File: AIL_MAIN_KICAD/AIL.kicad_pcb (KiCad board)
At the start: 2 copper layers, 71.9 x 33.4 mm, 25 parts, among them IC1 LT8315, J1 Conn_01x02_Female, J2 Conn_01x02_Female

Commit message: Updating main board
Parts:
- removed J1: Conn_01x02_Female, 2155760-1002:215760-YY02
- added D10: LED, AIL_MAIN_FOOT:LEDC2012X100N, B.Cu at (141.7, 92.2)
- added D11: LED, AIL_MAIN_FOOT:LEDC2012X100N, B.Cu at (146.3, 92.2)
- added D12: LED, AIL_MAIN_FOOT:LEDC2012X100N, B.Cu at (150.9, 92.2)
- added D13: LED, AIL_MAIN_FOOT:LEDC2012X100N, B.Cu at (155.7, 92.2)
- added D14: LED, AIL_MAIN_FOOT:LEDC2012X100N, B.Cu at (160.3, 92.2)
- added D15: LED, AIL_MAIN_FOOT:LEDC2012X100N, B.Cu at (141.7, 89.2)
- added D16: LED, AIL_MAIN_FOOT:LEDC2012X100N, B.Cu at (146.3, 89.2)
- added D17: LED, AIL_MAIN_FOOT:LEDC2012X100N, B.Cu at (150.9, 89.2)
- added D18: LED, AIL_MAIN_FOOT:LEDC2012X100N, B.Cu at (155.7, 89.2)
- added D19: LED, AIL_MAIN_FOOT:LEDC2012X100N, B.Cu at (160.3, 89.2)
- added D20: LED, AIL_MAIN_FOOT:LEDC2012X100N, B.Cu at (141.7, 86.1)
- added D21: LED, AIL_MAIN_FOOT:LEDC2012X100N, B.Cu at (146.3, 86.1)
- added D22: LED, AIL_MAIN_FOOT:LEDC2012X100N, B.Cu at (150.9, 86.1)
- added D23: LED, AIL_MAIN_FOOT:LEDC2012X100N, B.Cu at (155.7, 86.1)
- added D24: LED, AIL_MAIN_FOOT:LEDC2012X100N, B.Cu at (160.3, 86.1)
- added D25: LED, AIL_MAIN_FOOT:LEDC2012X100N, B.Cu at (141.7, 83.1)
- added D26: LED, AIL_MAIN_FOOT:LEDC2012X100N, B.Cu at (146.3, 83.1)
- added D27: LED, AIL_MAIN_FOOT:LEDC2012X100N, B.Cu at (150.9, 83.1)
- added D28: LED, AIL_MAIN_FOOT:LEDC2012X100N, B.Cu at (155.7, 83.1)
- added D29: LED, AIL_MAIN_FOOT:LEDC2012X100N, B.Cu at (160.3, 83.1)
- added D5: LED, AIL_MAIN_FOOT:LEDC2012X100N, B.Cu at (141.7, 95.2)
- added D6: LED, AIL_MAIN_FOOT:LEDC2012X100N, B.Cu at (146.3, 95.2)
- added D7: LED, AIL_MAIN_FOOT:LEDC2012X100N, B.Cu at (150.9, 95.2)
- added D8: LED, AIL_MAIN_FOOT:LEDC2012X100N, B.Cu at (155.7, 95.2)
- added D9: LED, AIL_MAIN_FOOT:LEDC2012X100N, B.Cu at (160.3, 95.2)
- added R8: 20, Resistor_SMD:R_0603_1608Metric_Pad0.98x0.95mm_HandSolder, B.Cu at (131.6, 96.2)
- added REF1: MountingHole_3mm, MountingHole:MountingHole_3mm, F.Cu at (122.0, 92.0)
- added REF2: MountingHole_3mm, MountingHole:MountingHole_3mm, F.Cu at (178.0, 79.0)
- added REF3: MountingHole_3mm, MountingHole:MountingHole_3mm, F.Cu at (178.0, 105.0)
- J2: footprint 2155760-1002:215760-YY02 -> Connector_Molex:Molex_Micro-Fit_3.0_43045-0200_2x01_P3.00mm_Horizontal
- moved C9 73.0 mm to (165.9, 95.0)
- moved C7 68.3 mm to (180.1, 88.2)
- moved R7 68.3 mm to (177.2, 88.2)
- moved R6 68.2 mm to (174.5, 86.3)
- moved D4 67.8 mm to (165.6, 84.1)
- moved C6 66.3 mm to (174.6, 92.2)
- moved R4 66.3 mm to (173.1, 94.8)
- moved R5 66.3 mm to (171.4, 87.5)
- moved IC1 65.7 mm to (166.5, 90.3)
- moved C4 65.0 mm to (178.2, 94.1), turned to 90 degrees
- moved R1 64.9 mm to (155.2, 91.7)
- moved R3 64.2 mm to (169.4, 95.0)
- moved C5 63.0 mm to (161.8, 91.7), turned to -90 degrees
- moved C3 62.0 mm to (151.7, 92.6), turned to -90 degrees
- moved C8 62.0 mm to (156.2, 88.1), turned to -90 degrees
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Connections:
- net /12V renamed +12V
- IC1 pad 15: unconnected-(IC1-Pad15) -> ICGND
- IC1 pad 2: unconnected-(IC1-Pad2) -> HV1
- IC1 pad 3: unconnected-(IC1-Pad3) -> HV1
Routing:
- net GND: track 37.0 -> 82.3 mm
- net HV1: track 61.1 -> 39.0 mm, vias 2 -> 0
- net Net-(C3-Pad1): track 27.8 -> 11.6 mm, vias 2 -> 0
- net Net-(C9-Pad1): track 16.0 -> 5.27 mm, vias 2 -> 0
- net Net-(D10-Pad2): track 0.00 -> 9.09 mm
- net ICGND: track 85.1 -> 76.1 mm
- net HV3: track 16.6 -> 24.2 mm
- net +12V: track 33.2 -> 30.1 mm, vias 2 -> 1
- net Net-(C7-Pad1): track 14.4 -> 11.5 mm
- net Net-(D7-Pad1): track 0.00 -> 2.73 mm
- net Net-(D27-Pad1): track 0.00 -> 2.73 mm
- net Net-(D22-Pad1): track 0.00 -> 2.73 mm
- net Net-(D17-Pad1): track 0.00 -> 2.73 mm
- net Net-(D12-Pad1): track 0.00 -> 2.73 mm
- net Net-(D8-Pad1): track 0.00 -> 2.47 mm
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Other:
- board size 71.9 x 33.4 mm -> 68 x 38 mm

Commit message: updating with BOM
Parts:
- added C3: 22uF, Capacitor_SMD:C_0805_2012Metric_Pad1.18x1.45mm_HandSolder, F.Cu at (130.6, 97.0)
- C1: footprint Capacitor_SMD:C_0603_1608Metric_Pad1.08x0.95mm_HandSolder -> Capacitor_SMD:C_1812_4532Metric_Pad1.57x3.40mm_HandSolder
- C2: value 43E-6 -> 22uF; footprint Capacitor_SMD:C_0603_1608Metric_Pad1.08x0.95mm_HandSolder -> Capacitor_SMD:C_0805_2012Metric_Pad1.18x1.45mm_HandSolder
- C4: footprint Capacitor_SMD:C_0603_1608Metric_Pad1.08x0.95mm_HandSolder -> Capacitor_SMD:C_01005_0402Metric_Pad0.57x0.30mm_HandSolder
- C9: value 100E-9 -> 10E-6
- R6: value 1.91E6 -> 1.87E6; footprint Resistor_SMD:R_0603_1608Metric_Pad0.98x0.95mm_HandSolder -> Capacitor_SMD:C_1206_3216Metric_Pad1.33x1.80mm_HandSolder
- moved C7 18.8 mm to (167.7, 102.3), turned to 180 degrees
- moved C4 17.0 mm to (162.1, 99.3), turned to 0 degrees
- moved REF1 15.2 mm to (128.0, 106.0)
- moved R7 14.7 mm to (167.7, 99.5), turned to 0 degrees
- moved R4 12.0 mm to (161.1, 95.4), turned to 90 degrees
- moved C6 11.9 mm to (163.6, 96.9), turned to 0 degrees
- moved R6 11.1 mm to (170.2, 96.5), turned to 0 degrees
- moved R3 9.10 mm to (160.9, 91.7), turned to -90 degrees
- moved C9 8.45 mm to (160.9, 88.2), turned to -90 degrees
- moved C5 7.98 mm to (164.2, 84.1), turned to 180 degrees
- moved D4 7.30 mm to (171.8, 87.9), turned to 90 degrees
- moved R2 7.21 mm to (167.8, 84.1), turned to 180 degrees
- moved R5 6.33 mm to (169.4, 93.5), turned to 0 degrees
- moved IC1 1.76 mm to (165.6, 88.8), turned to 180 degrees
- moved C2 1.71 mm to (130.6, 94.5)
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- renumbered C3 to C10
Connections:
- C7 pad 1: Net-(C7-Pad1) -> Net-(D4-Pad1)
- IC1 pad 17: Net-(C7-Pad1) -> Net-(IC1-Pad17)
- R6 pad 1: Net-(C7-Pad1) -> Net-(IC1-Pad17)
- R7 pad 2: Net-(C7-Pad1) -> Net-(IC1-Pad17)
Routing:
- net HV3: track 24.2 -> 8.34 mm
- net ICGND: track 76.1 -> 61.7 mm
- net Net-(D10-Pad2): track 9.09 -> 21.3 mm
- net Net-(C7-Pad1): track 11.5 -> 0.00 mm
- net HV2: track 20.3 -> 11.6 mm
- net Net-(IC1-Pad17): track 0.00 -> 8.61 mm
- net Net-(D4-Pad1): track 7.45 -> 13.9 mm
- net HV1: track 39.0 -> 44.3 mm
- net GND: track 82.3 -> 80.2 mm
- net Net-(C4-Pad1): track 4.22 -> 3.20 mm
- net Net-(IC1-Pad18): track 2.09 -> 3.03 mm
- net Net-(C9-Pad1): track 5.27 -> 4.53 mm
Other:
- board size 68 x 38 mm -> 61 x 38 mm

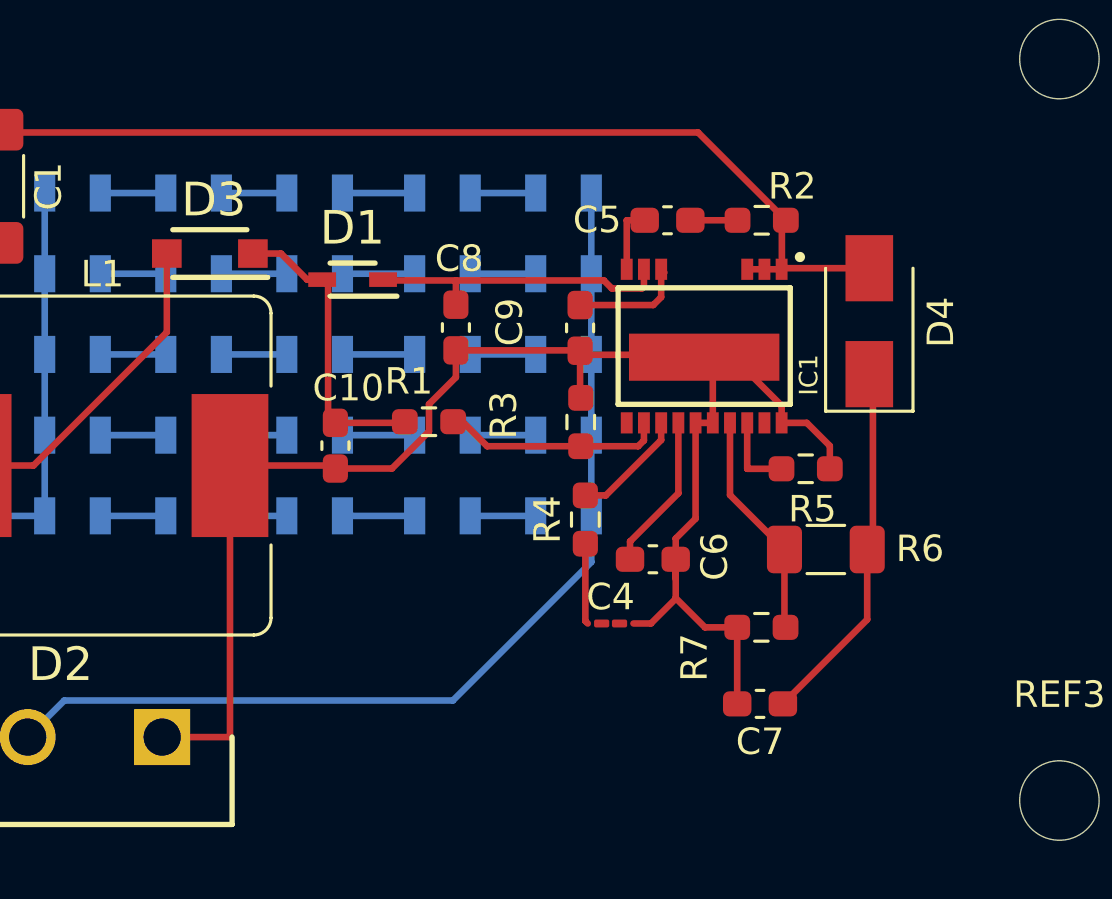
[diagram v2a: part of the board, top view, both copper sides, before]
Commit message: updating PCB with seperated BOMs
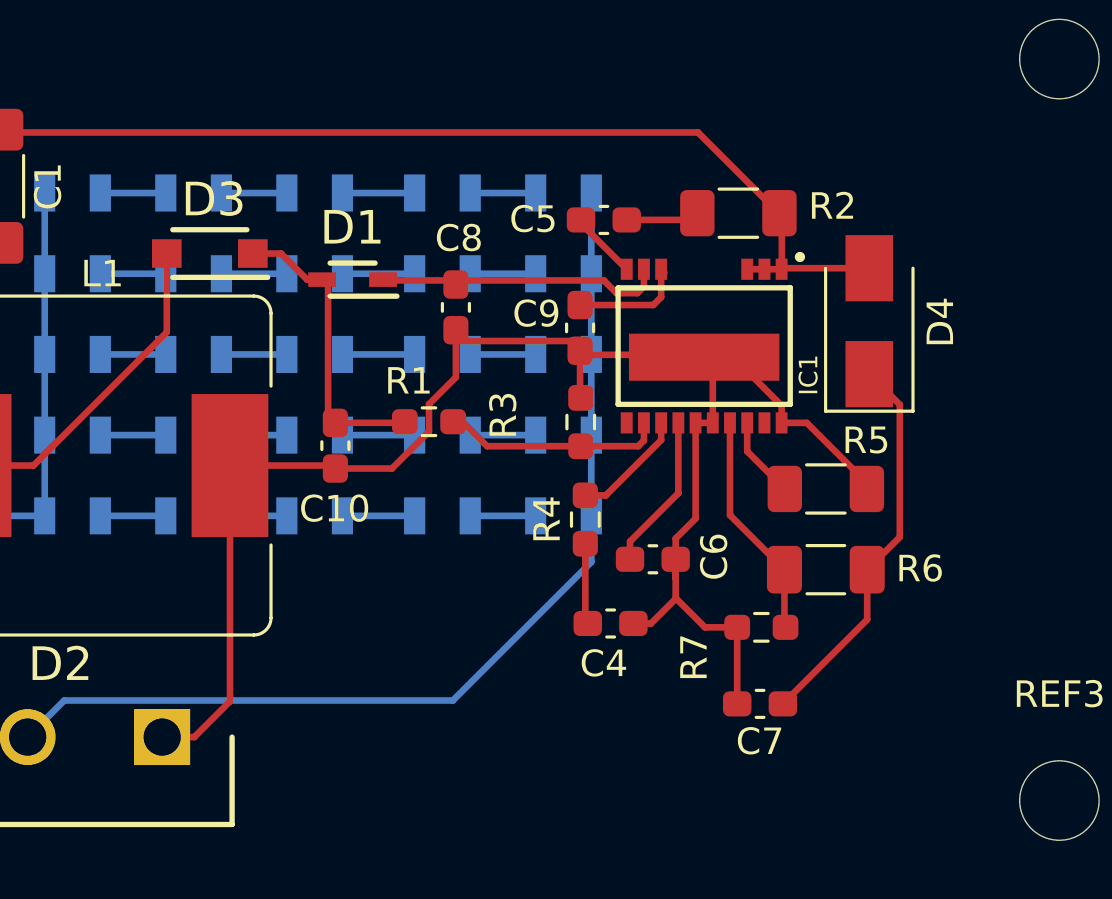
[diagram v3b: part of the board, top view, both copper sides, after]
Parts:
- C4: footprint Capacitor_SMD:C_01005_0402Metric_Pad0.57x0.30mm_HandSolder -> Capacitor_SMD:C_0603_1608Metric_Pad1.08x0.95mm_HandSolder
- R2, R5: footprint Resistor_SMD:R_0603_1608Metric_Pad0.98x0.95mm_HandSolder -> Resistor_SMD:R_1206_3216Metric_Pad1.30x1.75mm_HandSolder
- moved C5 2.40 mm to (161.8, 84.1)
- moved R5 1.08 mm to (170.2, 94.2)
- moved R2 0.92 mm to (166.9, 83.8)
- moved C8 0.76 mm to (156.2, 87.4)
- moved R6 0.76 mm to (170.2, 97.3)
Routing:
- net ICGND: track 61.7 -> 63.3 mm
- net Net-(C5-Pad1): track 1.78 -> 2.77 mm
- net Net-(C7-Pad1): track 13.9 -> 14.8 mm
- net HV2: track 11.6 -> 11.0 mm

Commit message: Final Update to PCB
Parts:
- moved C6 0.94 mm to (164.6, 96.9)
- moved R3 0.94 mm to (160.0, 91.9)
- moved D4 0.90 mm to (172.7, 87.9)
- moved C9 0.88 mm to (160.0, 88.2)
- moved R4 0.63 mm to (161.0, 96.0)
- moved C5 0.25 mm to (161.8, 83.8)
- moved D3 0.25 mm to (146.9, 85.1)
- moved R2 0.25 mm to (166.9, 83.6)
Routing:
- net Net-(C9-Pad1): track 4.53 -> 6.17 mm
- net HV1: track 44.3 -> 45.2 mm
- net ICGND: track 63.3 -> 64.0 mm

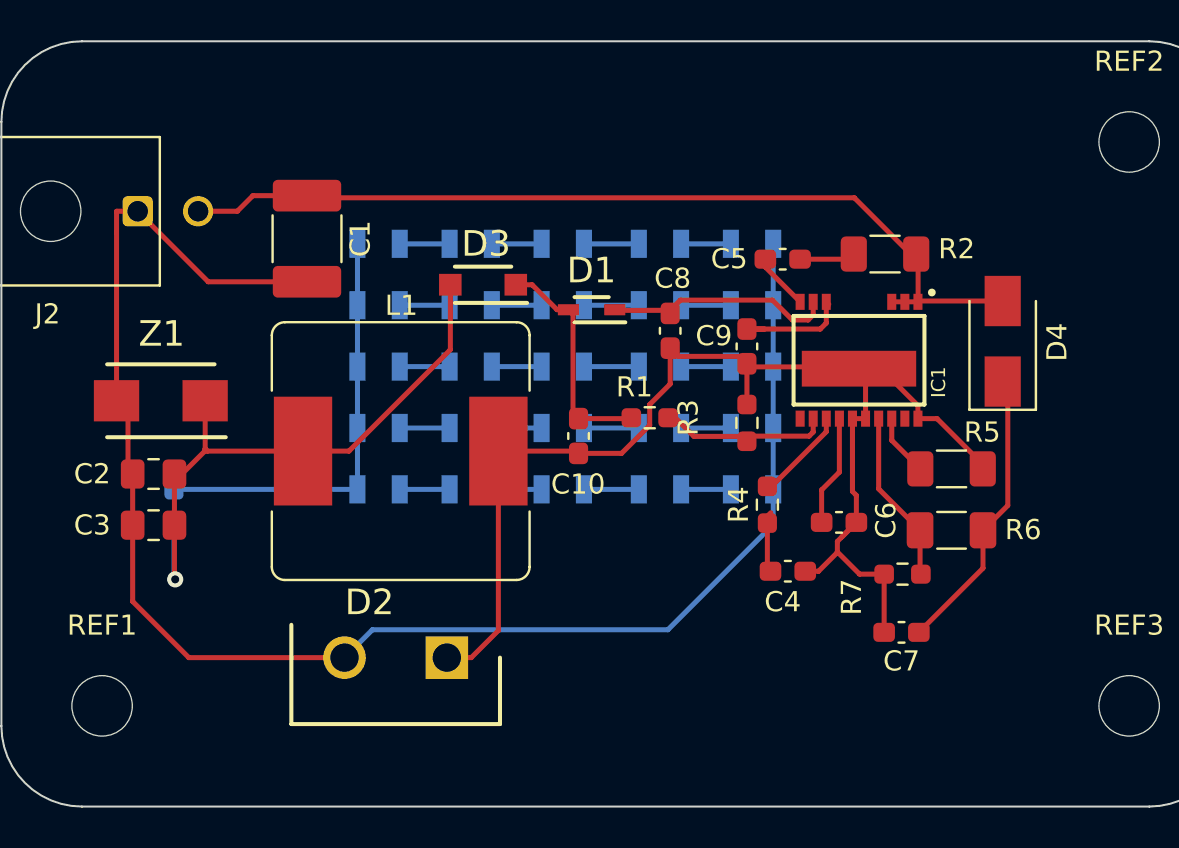
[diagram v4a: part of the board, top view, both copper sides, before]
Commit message: updating PCB with some logos
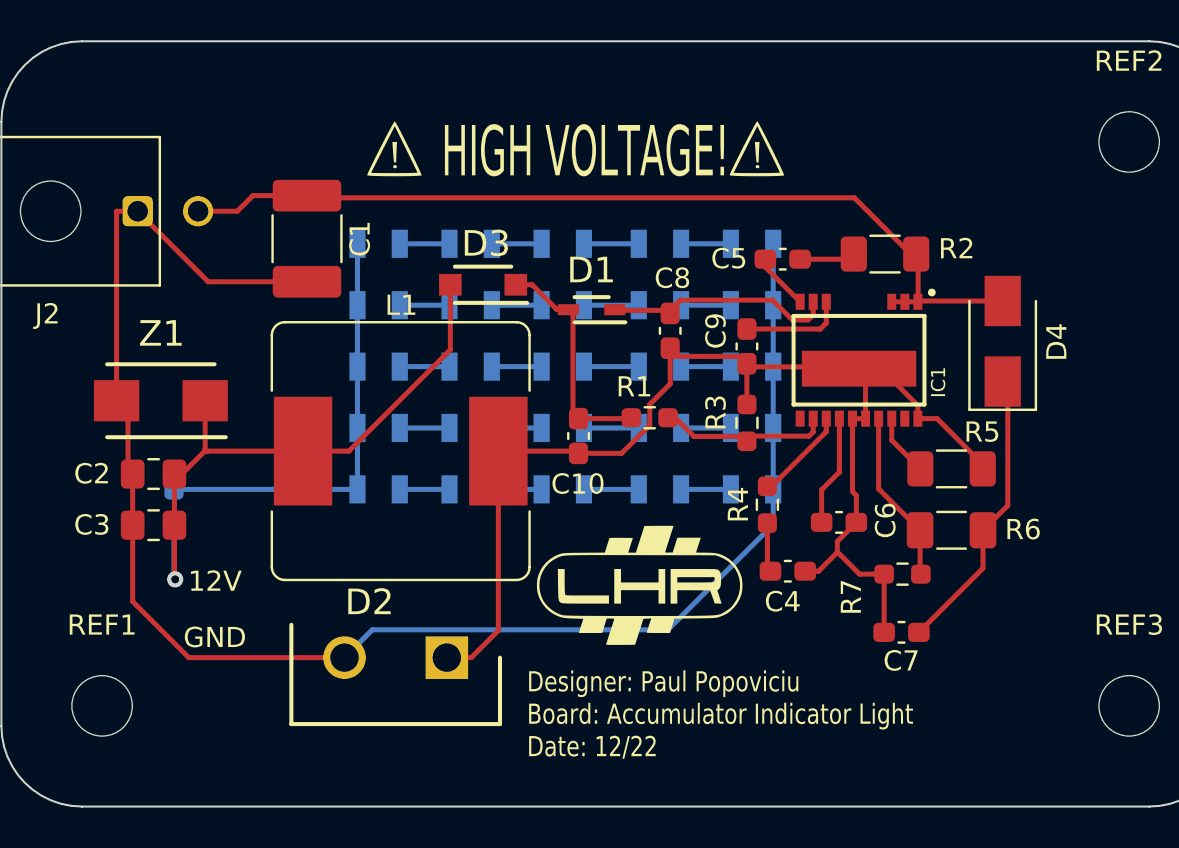
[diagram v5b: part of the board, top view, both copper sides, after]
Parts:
- added G***: LOGO, LOGO, F.Cu at (145.0, 80.0)
- added G***: LOGO, LOGO, F.Cu at (163.0, 80.0)
- added G***: LOGO, LOGO, F.Cu at (155.7, 101.1)
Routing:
- net Net-(C9-Pad1): track 6.17 -> 5.12 mm
- net ICGND: track 64.0 -> 63.0 mm
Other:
- board text added: "12V"
- board text added: "Designer: Paul Popoviciu Board: Accumulator Indicator Light Date: 12/22"
- board text added: "GND"
- board text added: "HIGH VOLTAGE!"

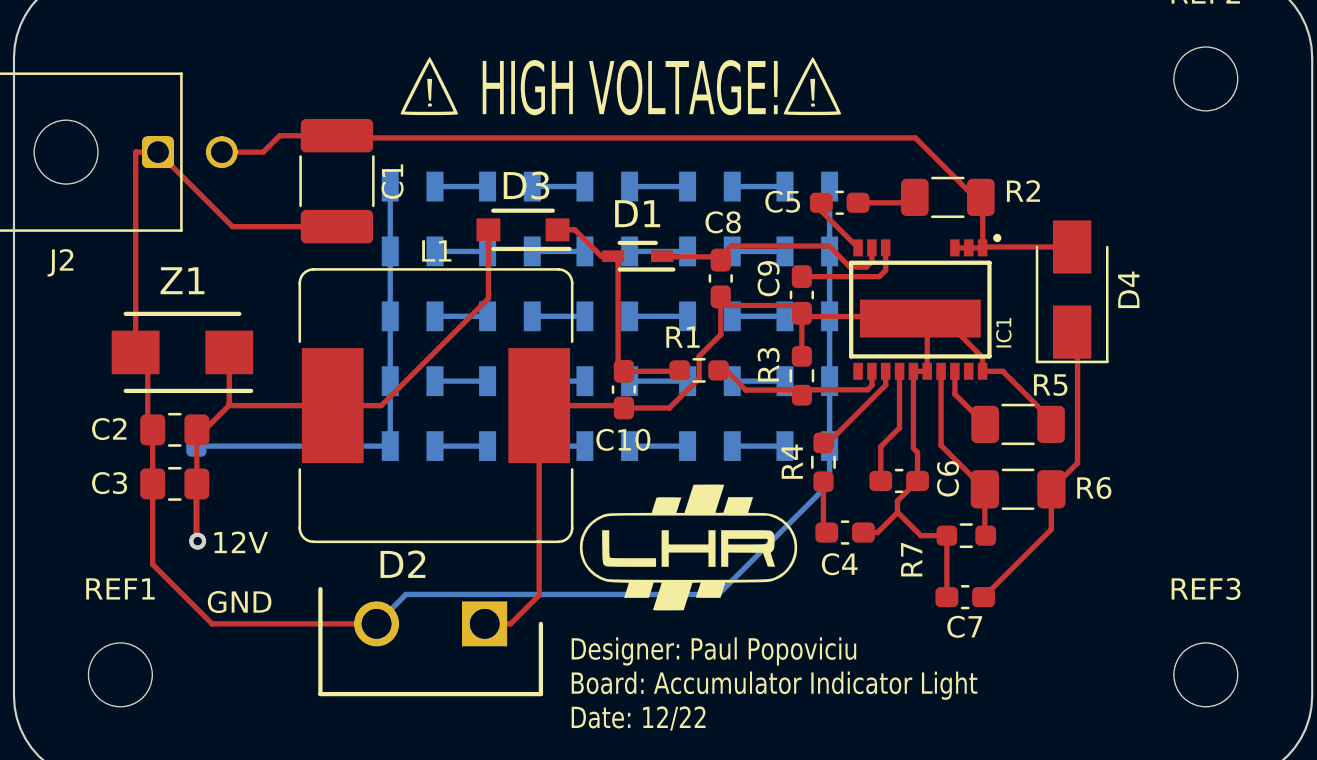
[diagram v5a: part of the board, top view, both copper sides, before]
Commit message: increasing size of high current paths
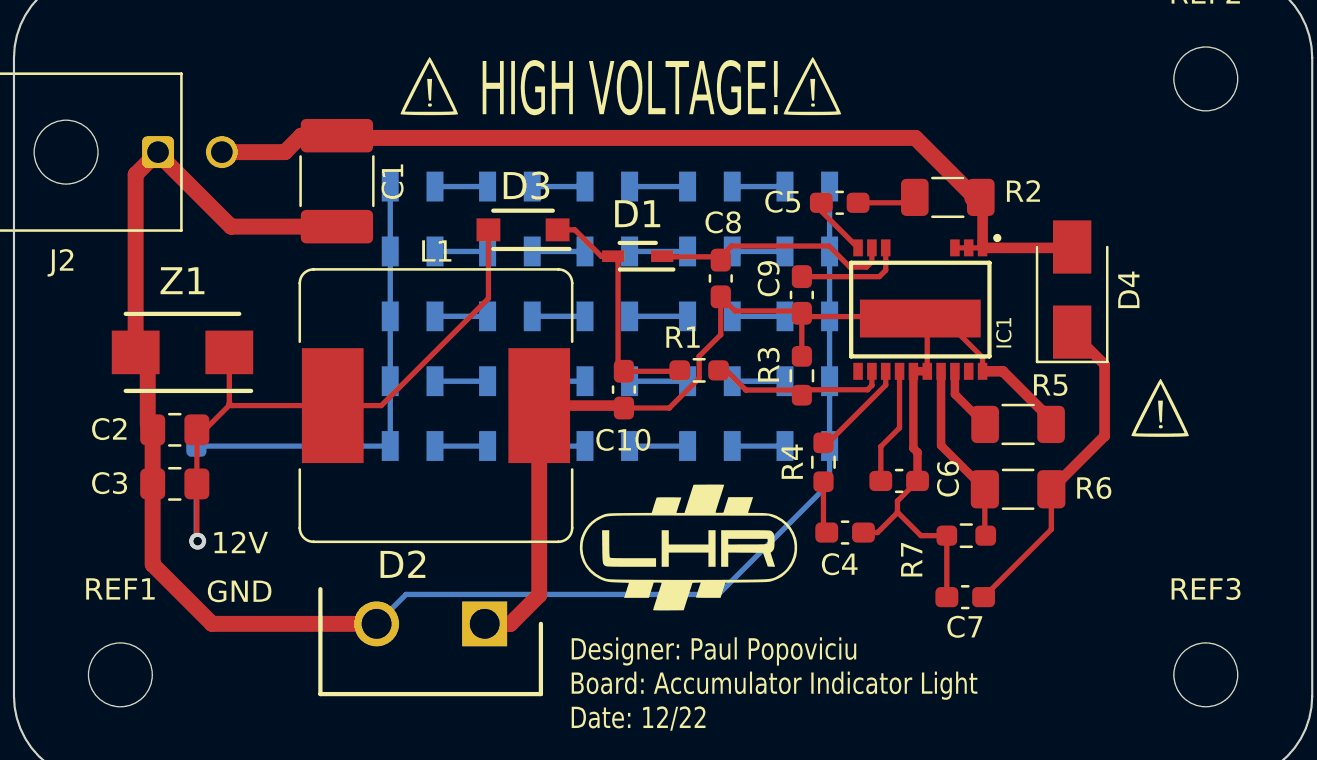
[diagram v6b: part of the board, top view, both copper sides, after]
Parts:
- added G***: LOGO, LOGO, F.Cu at (179.3, 95.1)
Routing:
- net Net-(C7-Pad1): track 14.4 -> 15.4 mm
- net GND: track 80.2 -> 79.7 mm
